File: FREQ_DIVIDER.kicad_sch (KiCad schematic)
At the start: 5 parts, among them U3 SRV05-4, U4 74VHC163FT

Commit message: Export
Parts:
- removed U3: SRV05-4, Package_TO_SOT_SMD:SOT-23-6, symbol Power_Protection:SRV05-4
- added D7: SRV05-4, Package_TO_SOT_SMD:SOT-23-6, symbol Power_Protection:NUP4202
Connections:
- net 5V: now also D7.5
- net GND: now also D7.2
- net at R8.1, U4.2 (CP): now also D7.4
- no-connect marks 4 -> 7
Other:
- moved on the sheet: R7, R8
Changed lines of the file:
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@@
   (junction (at 154.94 97.79) (diameter 0) (color 0 0 0 0)
   )
-  (junction (at 133.35 93.98) (diameter 0) (color 0 0 0 0)
-  )
-  (junction (at 106.68 93.98) (diameter 0) (color 0 0 0 0)
-  )
-  (junction (at 86.36 93.98) (diameter 0) (color 0 0 0 0)
-  )
-  (junction (at 133.35 74.93) (diameter 0) (color 0 0 0 0)
-  )
+  (junction (at 123.19 74.93) (diameter 0) (color 0 0 0 0)
+  )
+  (junction (at 86.36 74.93) (diameter 0) (color 0 0 0 0)
+  )
+  (no_connect (at 123.19 93.98))
+  (no_connect (at 118.11 83.82))
   (no_connect (at 189.23 87.63))
   (no_connect (at 189.23 92.71))
+  (no_connect (at 118.11 93.98))
   (no_connect (at 189.23 97.79))
   (no_connect (at 189.23 85.09))
-  (wire (pts (xy 120.65 83.82) (xy 120.65 63.5))
-    (stroke (width 0) (type default))
-  )
-  (wire (pts (xy 133.35 74.93) (xy 133.35 93.98))
+  (wire (pts (xy 120.65 63.5) (xy 120.65 83.82))
     (stroke (width 0) (type default))
   )
@@
     (stroke (width 0) (type default))
   )
-  (wire (pts (xy 106.68 74.93) (xy 106.68 93.98))
-    (stroke (width 0) (type default))
-  )
   (wire (pts (xy 163.83 87.63) (xy 163.83 90.17))
     (stroke (width 0) (type default))
@@
     (stroke (width 0) (type default))
   )
-  (wire (pts (xy 86.36 86.36) (xy 86.36 63.5))
+  (wire (pts (xy 86.36 67.31) (xy 86.36 63.5))
     (stroke (width 0) (type default))
   )
@@
     (stroke (width 0) (type default))
   )
-  (wire (pts (xy 81.28 93.98) (xy 86.36 93.98))
-    (stroke (width 0) (type default))
-  )
-  (wire (pts (xy 133.35 74.93) (xy 106.68 74.93))
-    (stroke (width 0) (type default))
-  )
-  (wire (pts (xy 106.68 93.98) (xy 106.68 99.06))
+  (wire (pts (xy 81.28 74.93) (xy 86.36 74.93))
+    (stroke (width 0) (type default))
+  )
+  (wire (pts (xy 101.6 74.93) (xy 123.19 74.93))
     (stroke (width 0) (type default))
   )
@@
     (stroke (width 0) (type default))
   )
-  (wire (pts (xy 106.68 93.98) (xy 107.95 93.98))
-    (stroke (width 0) (type default))
-  )
-  (wire (pts (xy 101.6 93.98) (xy 106.68 93.98))
-    (stroke (width 0) (type default))
-  )
   (wire (pts (xy 154.94 63.5) (xy 120.65 63.5))
     (stroke (width 0) (type default))
@@
     (stroke (width 0) (type default))
   )
-  (wire (pts (xy 86.36 93.98) (xy 93.98 93.98))
+  (wire (pts (xy 123.19 74.93) (xy 148.59 74.93))
+    (stroke (width 0) (type default))
+  )
+  (wire (pts (xy 86.36 74.93) (xy 93.98 74.93))
     (stroke (width 0) (type default))
   )
@@
     (stroke (width 0) (type default))
   )
+  (wire (pts (xy 123.19 74.93) (xy 123.19 83.82))
+    (stroke (width 0) (type default))
+  )
   (wire (pts (xy 86.36 63.5) (xy 80.01 63.5))
     (stroke (width 0) (type default))
@@
     (stroke (width 0) (type default))
   )
-  (wire (pts (xy 148.59 74.93) (xy 133.35 74.93))
-    (stroke (width 0) (type default))
-  )
-  (wire (pts (xy 106.68 99.06) (xy 107.95 99.06))
-    (stroke (width 0) (type default))
-  )
   (wire (pts (xy 163.83 90.17) (xy 163.83 92.71))
     (stroke (width 0) (type default))
@@
     (stroke (width 0) (type default))
   )
-  (wire (pts (xy 133.35 93.98) (xy 133.35 99.06))
-    (stroke (width 0) (type default))
-  )
   (wire (pts (xy 195.58 90.17) (xy 189.23 90.17))
     (stroke (width 0) (type default))
   )
-  (hierarchical_label "IN" (shape input) (at 81.28 93.98 180) (fields_autoplaced)
+  (hierarchical_label "IN" (shape input) (at 81.28 74.93 180) (fields_autoplaced)
     (effects (font (size 1.27 1.27)) (justify right))
   )
@@
     )
   )
-  (symbol (lib_id "power:GND") (at 120.65 109.22 0) (unit 1)
-    (in_bom yes) (on_board yes) (dnp no) (fields_autoplaced)
-    (property "Reference" "#PWR0162" (at 120.65 115.57 0)
-      (effects (font (size 1.27 1.27)) hide)
-    )
-    (property "Value" "GND" (at 120.65 113.7826 0)
-      (effects (font (size 1.27 1.27)))
-    )
-    (property "Footprint" "" (at 120.65 109.22 0)
-      (effects (font (size 1.27 1.27)) hide)
-    )
-    (property "Datasheet" "" (at 120.65 109.22 0)
+  (symbol (lib_id "power:GND") (at 120.65 93.98 0) (unit 1)
+    (in_bom yes) (on_board yes) (dnp no) (fields_autoplaced)
+    (property "Reference" "#PWR0162" (at 120.65 100.33 0)
+      (effects (font (size 1.27 1.27)) hide)
+    )
+    (property "Value" "GND" (at 120.65 98.5426 0)
+      (effects (font (size 1.27 1.27)))
+    )
+    (property "Footprint" "" (at 120.65 93.98 0)
+      (effects (font (size 1.27 1.27)) hide)
+    )
+    (property "Datasheet" "" (at 120.65 93.98 0)
       (effects (font (size 1.27 1.27)) hide)
     )
@@
     )
   )
-  (symbol (lib_id "Device:R") (at 97.79 93.98 270) (unit 1)
-    (in_bom yes) (on_board yes) (dnp no) (fields_autoplaced)
-    (property "Reference" "R8" (at 97.79 88.9974 90)
-      (effects (font (size 1.27 1.27)))
-    )
-    (property "Value" "4.7k" (at 97.79 91.7725 90)
-      (effects (font (size 1.27 1.27)))
-    )
-    (property "Footprint" "Resistor_SMD:R_0603_1608Metric_Pad0.98x0.95mm_HandSolder" (at 97.79 92.202 90)
-      (effects (font (size 1.27 1.27)) hide)
-    )
-    (property "Datasheet" "~" (at 97.79 93.98 0)
-      (effects (font (size 1.27 1.27)) hide)
-    )
-    (property "LCSC" "C23162" (at 97.79 93.98 0)
+  (symbol (lib_id "Power_Protection:NUP4202") (at 120.65 88.9 0) (unit 1)
+    (in_bom yes) (on_board yes) (dnp no)
+    (property "Reference" "D7" (at 109.855 88.265 90)
+      (effects (font (size 1.27 1.27)))
+    )
+    (property "Value" "SRV05-4" (at 112.395 88.265 90)
+      (effects (font (size 1.27 1.27)))
+    )
+    (property "Footprint" "Package_TO_SOT_SMD:SOT-23-6" (at 121.92 86.995 0)
+      (effects (font (size 1.27 1.27)) hide)
+    )
+    (property "Datasheet" "" (at 121.92 86.995 0)
+      (effects (font (size 1.27 1.27)) hide)
+    )
+    (property "LCSC" "C85364" (at 120.65 88.9 0)
+      (effects (font (size 1.27 1.27)) hide)
+    )
+    (pin "1")
+    (pin "2")
+    (pin "3")
+    (pin "4")
+    (pin "5")
+    (pin "6")
+    (instances
+      (project "GDI-4ch"
+        (path "/03caada9-9e22-4e2d-9035-b15433dfbb17"
+          (reference "D7") (unit 1)
+        )
+      )
+      (project "hellen-112-17"
+        (path "/ac264c30-3e9a-4be2-b97a-9949b68bd497/4c18ad5a-e515-4d0e-8406-9c9f532a0b7e"
+          (reference "D10") (unit 1)
+        )
+        (path "/ac264c30-3e9a-4be2-b97a-9949b68bd497/a574a284-d906-413f-999c-1439b6faa556"
+          (reference "D12") (unit 1)
+        )
+      )
+    )
+  )
+  (symbol (lib_id "Device:R") (at 97.79 74.93 270) (unit 1)
+    (in_bom yes) (on_board yes) (dnp no) (fields_autoplaced)
+    (property "Reference" "R8" (at 97.79 69.9474 90)
+      (effects (font (size 1.27 1.27)))
+    )
+    (property "Value" "4.7k" (at 97.79 72.7225 90)
+      (effects (font (size 1.27 1.27)))
+    )
+    (property "Footprint" "Resistor_SMD:R_0603_1608Metric_Pad0.98x0.95mm_HandSolder" (at 97.79 73.152 90)
+      (effects (font (size 1.27 1.27)) hide)
+    )
+    (property "Datasheet" "~" (at 97.79 74.93 0)
+      (effects (font (size 1.27 1.27)) hide)
+    )
+    (property "LCSC" "C23162" (at 97.79 74.93 0)
       (effects (font (size 1.27 1.27)) hide)
     )
@@
     )
   )
-  (symbol (lib_id "Power_Protection:SRV05-4") (at 120.65 96.52 0) (unit 1)
-    (in_bom yes) (on_board yes) (dnp no)
-    (property "Reference" "U3" (at 114.3 85.0604 0)
-      (effects (font (size 1.27 1.27)))
-    )
-    (property "Value" "SRV05-4" (at 127 85.2955 0)
-      (effects (font (size 1.27 1.27)))
-    )
-    (property "Footprint" "Package_TO_SOT_SMD:SOT-23-6" (at 138.43 107.95 0)
-      (effects (font (size 1.27 1.27)) hide)
-    )
-    (property "Datasheet" "http://www.onsemi.com/pub/Collateral/SRV05-4-D.PDF" (at 120.65 96.52 0)
-      (effects (font (size 1.27 1.27)) hide)
-    )
-    (property "LCSC" "C85364" (at 120.65 96.52 0)
-      (effects (font (size 1.27 1.27)) hide)
-    )
-    (pin "1")
-    (pin "2")
-    (pin "3")
-    (pin "4")
-    (pin "5")
-    (pin "6")
-    (instances
-      (project "frequency-divider"
-        (path "/63d2dd9f-d5ff-4811-a88d-0ba932475460"
-          (reference "U3") (unit 1)
-        )
-      )
-      (project "hellen-112-17"
-        (path "/ac264c30-3e9a-4be2-b97a-9949b68bd497/a574a284-d906-413f-999c-1439b6faa556"
-          (reference "U6") (unit 1)
-        )
-      )
-    )
-  )
-  (symbol (lib_id "Device:R") (at 86.36 90.17 180) (unit 1)
-    (in_bom yes) (on_board yes) (dnp no) (fields_autoplaced)
-    (property "Reference" "R7" (at 88.1381 89.2615 0)
+  (symbol (lib_id "Device:R") (at 86.36 71.12 180) (unit 1)
+    (in_bom yes) (on_board yes) (dnp no) (fields_autoplaced)
+    (property "Reference" "R7" (at 88.1381 70.2115 0)
       (effects (font (size 1.27 1.27)) (justify right))
     )
-    (property "Value" "4.7k" (at 88.1381 92.0366 0)
+    (property "Value" "4.7k" (at 88.1381 72.9866 0)
       (effects (font (size 1.27 1.27)) (justify right))
     )
-    (property "Footprint" "Resistor_SMD:R_0603_1608Metric_Pad0.98x0.95mm_HandSolder" (at 88.138 90.17 90)
-      (effects (font (size 1.27 1.27)) hide)
-    )
-    (property "Datasheet" "~" (at 86.36 90.17 0)
-      (effects (font (size 1.27 1.27)) hide)
-    )
-    (property "LCSC" "C23162" (at 86.36 90.17 0)
-      (effects (font (size 1.27 1.27)) hide)
-    )
+    (property "Footprint" "Resistor_SMD:R_0603_1608Metric_Pad0.98x0.95mm_HandSolder" (at 88.138 71.12 90)
+      (effects (font (size 1.27 1.27)) hide)
+    )
+    (property "Datasheet" "~" (at 86.36 71.12 0)
+      (effects (font (size 1.27 1.27)) hide)
+    )
+    (property "LCSC" "C23162" (at 86.36 71.12 0)
+      (effects (font (size 1.27 1.27)) hide)
+    )

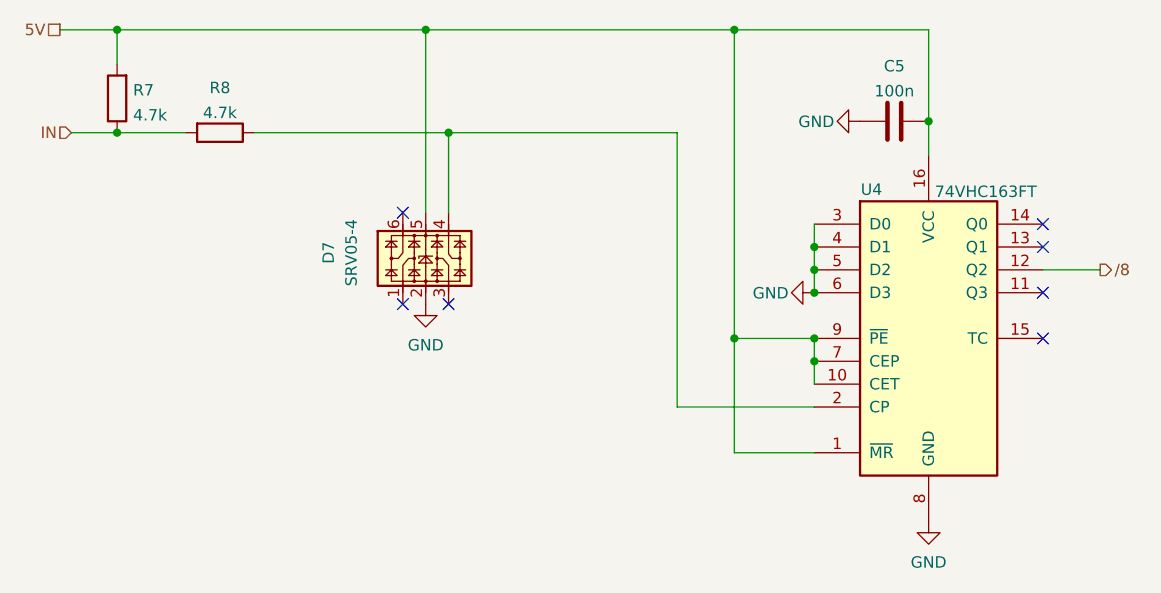
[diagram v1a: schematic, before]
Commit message: srv05 value fix
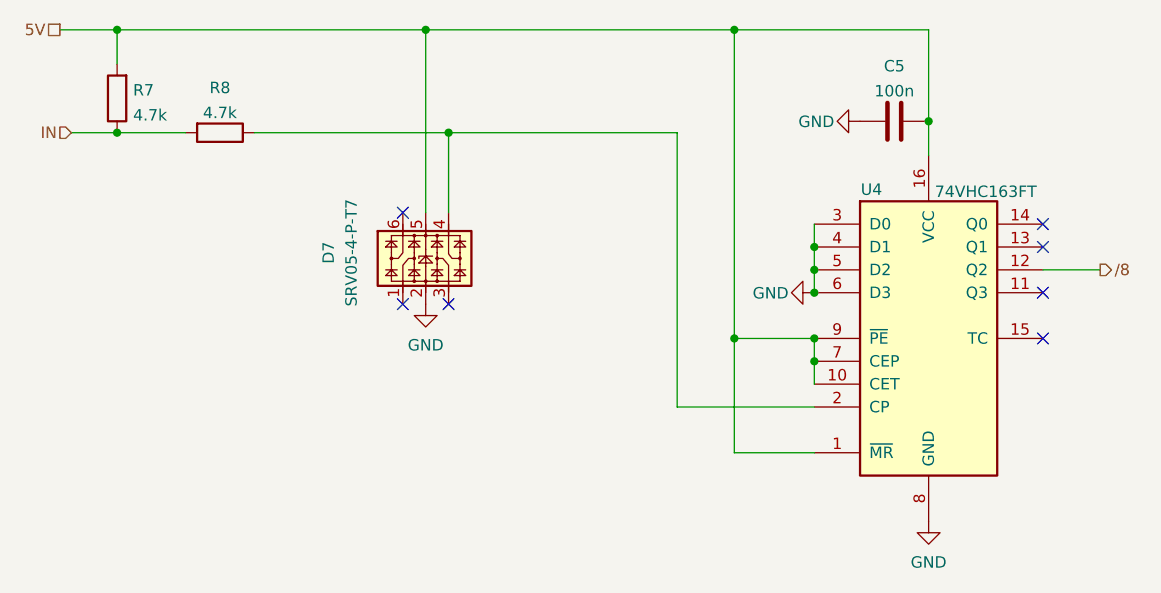
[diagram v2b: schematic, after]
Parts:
- D7: value SRV05-4 -> SRV05-4-P-T7
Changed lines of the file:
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@@
       (effects (font (size 1.27 1.27)))
     )
-    (property "Value" "SRV05-4" (at 112.395 88.265 90)
+    (property "Value" "SRV05-4-P-T7" (at 112.395 88.265 90)
       (effects (font (size 1.27 1.27)))
     )

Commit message: Warnings fix
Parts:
- removed R7, R8: 4.7k, Resistor_SMD:R_0603_1608Metric_Pad0.98x0.95mm_HandSolder, symbol Device:R
- added R30 (x2): 4.7k, hellen-one-common:R0603, symbol hellen-one-common:Res
- C5: footprint Capacitor_SMD:C_0603_1608Metric_Pad1.08x0.95mm_HandSolder -> hellen-one-common:C0603
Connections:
- net 5V: now also R30.2
- net IN: now also R30.1, R30.2
- net at D7.4, U4.2 (CP): now also R30.1
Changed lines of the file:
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@@
 (kicad_sch (version 20230121) (generator eeschema)
   (paper "A4")
+  (junction (at 88.9 74.93) (diameter 0) (color 0 0 0 0)
+  )
   (junction (at 154.94 63.5) (diameter 0) (color 0 0 0 0)
   )
@@
   (junction (at 163.83 97.79) (diameter 0) (color 0 0 0 0)
   )
-  (junction (at 86.36 63.5) (diameter 0) (color 0 0 0 0)
-  )
   (junction (at 163.83 87.63) (diameter 0) (color 0 0 0 0)
   )
@@
   (junction (at 176.53 73.66) (diameter 0) (color 0 0 0 0)
   )
+  (junction (at 88.9 63.5) (diameter 0) (color 0 0 0 0)
+  )
   (junction (at 163.83 92.71) (diameter 0) (color 0 0 0 0)
   )
@@
   )
   (junction (at 123.19 74.93) (diameter 0) (color 0 0 0 0)
-  )
-  (junction (at 86.36 74.93) (diameter 0) (color 0 0 0 0)
   )
   (no_connect (at 123.19 93.98))
@@
     (stroke (width 0) (type default))
   )
+  (wire (pts (xy 81.28 74.93) (xy 88.9 74.93))
+    (stroke (width 0) (type default))
+  )
   (wire (pts (xy 163.83 87.63) (xy 163.83 90.17))
     (stroke (width 0) (type default))
   )
+  (wire (pts (xy 88.9 74.93) (xy 91.44 74.93))
+    (stroke (width 0) (type default))
+  )
   (wire (pts (xy 163.83 110.49) (xy 154.94 110.49))
     (stroke (width 0) (type default))
   )
-  (wire (pts (xy 86.36 67.31) (xy 86.36 63.5))
-    (stroke (width 0) (type default))
-  )
   (wire (pts (xy 163.83 85.09) (xy 163.83 87.63))
     (stroke (width 0) (type default))
   )
-  (wire (pts (xy 120.65 63.5) (xy 86.36 63.5))
+  (wire (pts (xy 80.01 63.5) (xy 88.9 63.5))
     (stroke (width 0) (type default))
   )
@@
     (stroke (width 0) (type default))
   )
-  (wire (pts (xy 81.28 74.93) (xy 86.36 74.93))
-    (stroke (width 0) (type default))
-  )
   (wire (pts (xy 101.6 74.93) (xy 123.19 74.93))
     (stroke (width 0) (type default))
@@
     (stroke (width 0) (type default))
   )
-  (wire (pts (xy 86.36 74.93) (xy 93.98 74.93))
-    (stroke (width 0) (type default))
-  )
   (wire (pts (xy 163.83 97.79) (xy 163.83 100.33))
     (stroke (width 0) (type default))
@@
     (stroke (width 0) (type default))
   )
-  (wire (pts (xy 86.36 63.5) (xy 80.01 63.5))
+  (wire (pts (xy 88.9 63.5) (xy 120.65 63.5))
     (stroke (width 0) (type default))
   )
   (wire (pts (xy 163.83 105.41) (xy 148.59 105.41))
+    (stroke (width 0) (type default))
+  )
+  (wire (pts (xy 88.9 73.66) (xy 88.9 74.93))
     (stroke (width 0) (type default))
   )
@@
       (effects (font (size 1.27 1.27)))
     )
-    (property "Footprint" "Capacitor_SMD:C_0603_1608Metric_Pad1.08x0.95mm_HandSolder" (at 176.53 72.6948 0)
+    (property "Footprint" "hellen-one-common:C0603" (at 176.53 72.6948 0)
       (effects (font (size 1.27 1.27)) hide)
     )
@@
         (path "/ac264c30-3e9a-4be2-b97a-9949b68bd497/a574a284-d906-413f-999c-1439b6faa556"
           (reference "C14") (unit 1)
+        )
+      )
+    )
+  )
+  (symbol (lib_id "hellen-one-common:Res") (at 88.9 73.66 90) (unit 1)
+    (in_bom yes) (on_board yes) (dnp no)
+    (property "Reference" "R30" (at 86.36 68.58 0)
+      (effects (font (size 1.27 1.27)))
+    )
+    (property "Value" "4.7k" (at 88.9 68.58 0)
+      (effects (font (size 1.27 1.27)))
+    )
+    (property "Footprint" "hellen-one-common:R0603" (at 92.71 69.85 0)
+      (effects (font (size 1.27 1.27)) hide)
+    )
+    (property "Datasheet" "" (at 88.9 73.66 0)
+      (effects (font (size 1.27 1.27)) hide)
+    )
+    (property "LCSC" "C23162" (at 88.9 73.66 0)
+      (effects (font (size 1.27 1.27)) hide)
+    )
+    (pin "1")
+    (pin "2")
+    (instances
+      (project "alphax_8ch"
+        (path "/63d2dd9f-d5ff-4811-a88d-0ba932475460"
+          (reference "R30") (unit 1)
+        )
+        (path "/63d2dd9f-d5ff-4811-a88d-0ba932475460/9f286606-17ad-4292-b95a-d7d4de96430a"
+          (reference "R66") (unit 1)
+        )
+      )
+      (project "hellen-112-17"
+        (path "/ac264c30-3e9a-4be2-b97a-9949b68bd497/f1c1ee9f-24e7-4de8-a007-178b12809e45"
+          (reference "R34") (unit 1)
+        )
+        (path "/ac264c30-3e9a-4be2-b97a-9949b68bd497/a574a284-d906-413f-999c-1439b6faa556"
+          (reference "R19") (unit 1)
         )
       )
@@
         (path "/ac264c30-3e9a-4be2-b97a-9949b68bd497/a574a284-d906-413f-999c-1439b6faa556"
           (reference "D12") (unit 1)
-        )
-      )
-    )
-  )
-  (symbol (lib_id "Device:R") (at 97.79 74.93 270) (unit 1)
-    (in_bom yes) (on_board yes) (dnp no) (fields_autoplaced)
-    (property "Reference" "R8" (at 97.79 69.9474 90)
-      (effects (font (size 1.27 1.27)))
-    )
-    (property "Value" "4.7k" (at 97.79 72.7225 90)
-      (effects (font (size 1.27 1.27)))
-    )
-    (property "Footprint" "Resistor_SMD:R_0603_1608Metric_Pad0.98x0.95mm_HandSolder" (at 97.79 73.152 90)
-      (effects (font (size 1.27 1.27)) hide)
-    )
-    (property "Datasheet" "~" (at 97.79 74.93 0)
-      (effects (font (size 1.27 1.27)) hide)
-    )
-    (property "LCSC" "C23162" (at 97.79 74.93 0)
-      (effects (font (size 1.27 1.27)) hide)
-    )
-    (pin "1")
-    (pin "2")
-    (instances
-      (project "frequency-divider"
-        (path "/63d2dd9f-d5ff-4811-a88d-0ba932475460"
-          (reference "R8") (unit 1)
-        )
-      )
-      (project "hellen-112-17"
-        (path "/ac264c30-3e9a-4be2-b97a-9949b68bd497/a574a284-d906-413f-999c-1439b6faa556"
-          (reference "R20") (unit 1)
         )
       )
@@
     )
   )
-  (symbol (lib_id "Device:R") (at 86.36 71.12 180) (unit 1)
-    (in_bom yes) (on_board yes) (dnp no) (fields_autoplaced)
-    (property "Reference" "R7" (at 88.1381 70.2115 0)
-      (effects (font (size 1.27 1.27)) (justify right))
-    )
-    (property "Value" "4.7k" (at 88.1381 72.9866 0)
-      (effects (font (size 1.27 1.27)) (justify right))
-    )
-    (property "Footprint" "Resistor_SMD:R_0603_1608Metric_Pad0.98x0.95mm_HandSolder" (at 88.138 71.12 90)
-      (effects (font (size 1.27 1.27)) hide)
-    )
-    (property "Datasheet" "~" (at 86.36 71.12 0)
-      (effects (font (size 1.27 1.27)) hide)
-    )
-    (property "LCSC" "C23162" (at 86.36 71.12 0)
+  (symbol (lib_id "hellen-one-common:Res") (at 101.6 74.93 0) (mirror y) (unit 1)
+    (in_bom yes) (on_board yes) (dnp no)
+    (property "Reference" "R30" (at 96.52 72.39 0)
+      (effects (font (size 1.27 1.27)))
+    )
+    (property "Value" "4.7k" (at 96.52 74.93 0)
+      (effects (font (size 1.27 1.27)))
+    )
+    (property "Footprint" "hellen-one-common:R0603" (at 97.79 78.74 0)
+      (effects (font (size 1.27 1.27)) hide)
+    )
+    (property "Datasheet" "" (at 101.6 74.93 0)
+      (effects (font (size 1.27 1.27)) hide)
+    )
+    (property "LCSC" "C23162" (at 101.6 74.93 0)
       (effects (font (size 1.27 1.27)) hide)
     )
@@
     (pin "2")
     (instances
-      (project "frequency-divider"
-        (path "/63d2dd9f-d5ff-4811-a88d-0ba932475460"
-          (reference "R7") (unit 1)
-        )
-      )
-      (project "hellen-112-17"
-        (path "/ac264c30-3e9a-4be2-b97a-9949b68bd497/a574a284-d906-413f-999c-1439b6faa556"
-          (reference "R19") (unit 1)
-        )
-      )
+      (project "alphax_8ch"
+        (path "/63d2dd9f-d5ff-4811-a88d-0ba932475460"
+          (reference "R30") (unit 1)
+        )
+        (path "/63d2dd9f-d5ff-4811-a88d-0ba932475460/9f286606-17ad-4292-b95a-d7d4de96430a"
+          (reference "R66") (unit 1)
+        )
+      )
+      (project "hellen-112-17"
+        (path "/ac264c30-3e9a-4be2-b97a-9949b68bd497/f1c1ee9f-24e7-4de8-a007-178b12809e45"
+          (reference "R34") (unit 1)
+        )
+        (path "/ac264c30-3e9a-4be2-b97a-9949b68bd497/a574a284-d906-413f-999c-1439b6faa556"
+          (reference "R20") (unit 1)
+        )
+      )
